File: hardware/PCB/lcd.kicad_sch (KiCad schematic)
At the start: 68 parts, among them U1 TSC2013QRSARQ1, U2 TPS923650

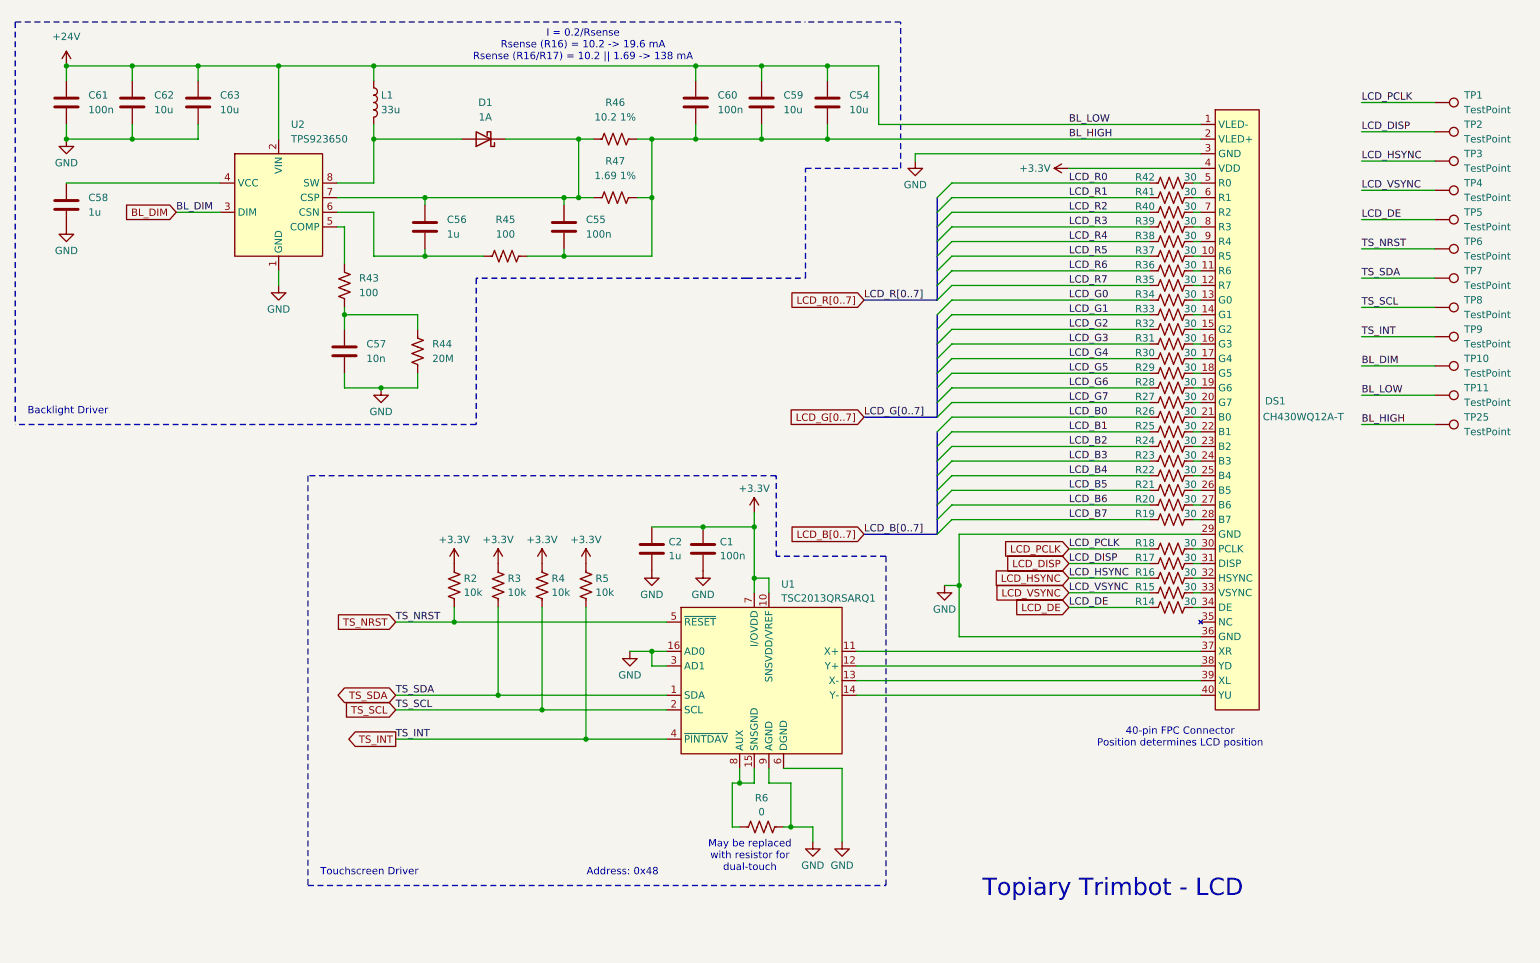
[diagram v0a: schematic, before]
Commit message: LCD schematic: small changes, add PSpice sim
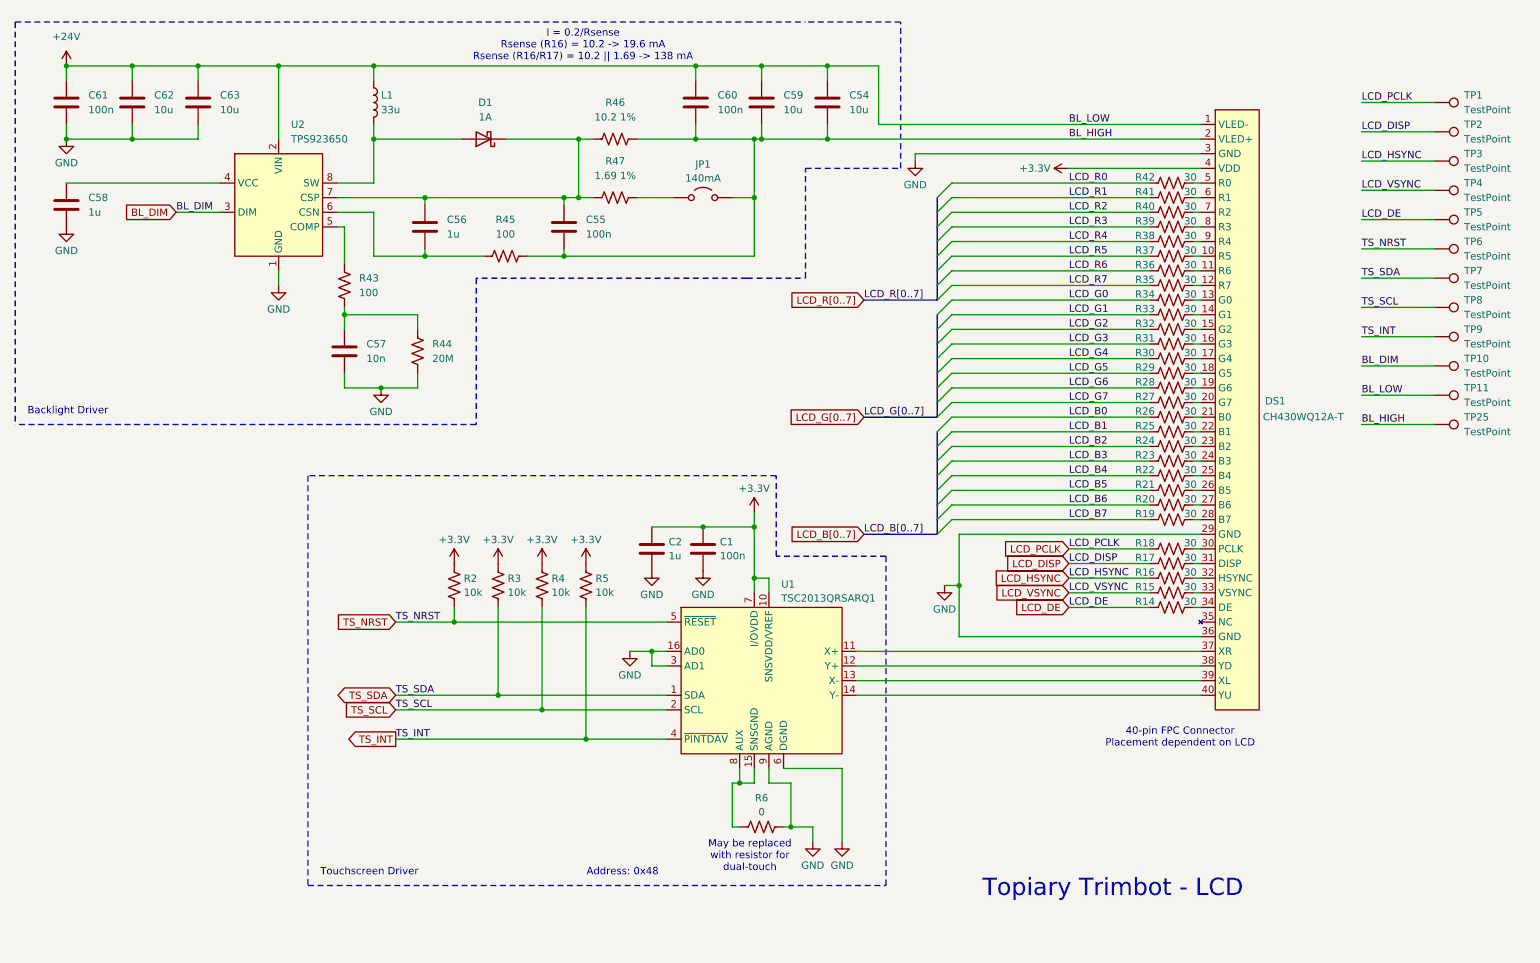
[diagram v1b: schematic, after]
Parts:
- added JP1: 140mA, symbol Jumper:Jumper_2_Open
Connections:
- net BL_HIGH: now also JP1.2 (B); no longer R47.2
- new net: JP1.1 (A), R47.2
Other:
- note added: "40-pin FPC Connector Placement dependent on LCD"
- note removed: "40-pin FPC Connector Position determines LCD position"
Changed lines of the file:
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@@
 		)
 	)
-	(text "40-pin FPC Connector\nPosition determines LCD position"
+	(text "40-pin FPC Connector\nPlacement dependent on LCD"
 		(exclude_from_sim no)
 		(at 222.504 148.336 0)
@@
 	)
 	(junction
+		(at 148.59 54.61)
+		(diameter 0)
+		(color 0 0 0 0)
+	)
+	(junction
 		(at 161.29 31.75)
 		(diameter 0)
@@
 	)
 	(junction
+		(at 148.59 44.45)
+		(diameter 0)
+		(color 0 0 0 0)
+	)
+	(junction
 		(at 118.11 44.45)
 		(diameter 0)
@@
 	)
 	(junction
-		(at 130.81 54.61)
-		(diameter 0)
-		(color 0 0 0 0)
-	)
-	(junction
 		(at 119.38 148.59)
 		(diameter 0)
@@
 	)
 	(junction
-		(at 130.81 44.45)
-		(diameter 0)
-		(color 0 0 0 0)
-	)
-	(junction
 		(at 40.64 31.75)
 		(diameter 0)
@@
 	(wire
 		(pts
-			(xy 128.27 44.45) (xy 130.81 44.45)
+			(xy 128.27 44.45) (xy 138.43 44.45)
 		)
 		(stroke
@@
 	(wire
 		(pts
+			(xy 138.43 44.45) (xy 148.59 44.45)
+		)
+		(stroke
+			(width 0)
+			(type default)
+		)
+	)
+	(wire
+		(pts
 			(xy 166.37 140.97) (xy 226.06 140.97)
 		)
@@
 	(wire
 		(pts
-			(xy 138.43 44.45) (xy 149.86 44.45)
-		)
-		(stroke
-			(width 0)
-			(type default)
-		)
-	)
-	(wire
-		(pts
 			(xy 184.15 121.92) (xy 184.15 130.81)
 		)
@@
 	(wire
 		(pts
-			(xy 115.57 64.77) (xy 130.81 64.77)
+			(xy 115.57 64.77) (xy 148.59 64.77)
 		)
 		(stroke
@@
 	(wire
 		(pts
-			(xy 130.81 44.45) (xy 138.43 44.45)
-		)
-		(stroke
-			(width 0)
-			(type default)
-		)
-	)
-	(wire
-		(pts
 			(xy 76.2 59.69) (xy 77.47 59.69)
 		)
@@
 		)
 	)
+	(wire
+		(pts
+			(xy 144.78 54.61) (xy 148.59 54.61)
+		)
+		(stroke
+			(width 0)
+			(type default)
+		)
+	)
 	(polyline
 		(pts
@@
 	(wire
 		(pts
-			(xy 130.81 54.61) (xy 130.81 44.45)
+			(xy 148.59 44.45) (xy 148.59 54.61)
 		)
 		(stroke
@@
 		)
 	)
+	(wire
+		(pts
+			(xy 148.59 44.45) (xy 149.86 44.45)
+		)
+		(stroke
+			(width 0)
+			(type default)
+		)
+	)
 	(bus
 		(pts
@@
 	(wire
 		(pts
+			(xy 148.59 54.61) (xy 148.59 64.77)
+		)
+		(stroke
+			(width 0)
+			(type default)
+		)
+	)
+	(wire
+		(pts
 			(xy 224.79 105.41) (xy 226.06 105.41)
 		)
@@
 	(wire
 		(pts
-			(xy 130.81 64.77) (xy 130.81 54.61)
-		)
-		(stroke
-			(width 0)
-			(type default)
-		)
-	)
-	(wire
-		(pts
 			(xy 77.47 73.66) (xy 77.47 74.93)
 		)
@@
 		)
 	)
-	(wire
-		(pts
-			(xy 128.27 54.61) (xy 130.81 54.61)
-		)
-		(stroke
-			(width 0)
-			(type default)
-		)
-	)
 	(polyline
 		(pts
@@
 	(wire
 		(pts
+			(xy 128.27 54.61) (xy 134.62 54.61)
+		)
+		(stroke
+			(width 0)
+			(type default)
+		)
+	)
+	(wire
+		(pts
 			(xy 148.59 111.76) (xy 148.59 120.65)
 		)
@@
 					(unit 1)
 				)
+			)
+		)
+	)
+	(symbol
+		(lib_id "Jumper:Jumper_2_Open")
+		(at 139.7 54.61 0)
+		(unit 1)
+		(exclude_from_sim no)
+		(in_bom yes)
+		(on_board yes)
+		(dnp no)
+		(fields_autoplaced yes)
+		(property "Reference" "JP1"
+			(at 139.7 48.8145 0)
+			(effects
+				(font
+					(size 1.27 1.27)
+				)
+			)
+		)
+		(property "Value" "140mA"
+			(at 139.7 51.2388 0)
+			(effects
+				(font
+					(size 1.27 1.27)
+				)
+			)
+		)
+		(property "Footprint" ""
+			(at 139.7 54.61 0)
+			(effects
+				(font
+					(size 1.27 1.27)
+				)
+				(hide yes)
+			)
+		)
+		(property "Datasheet" "~"
+			(at 139.7 54.61 0)
+			(effects
+				(font
+					(size 1.27 1.27)
+				)
+				(hide yes)
+			)
+		)
+		(property "Description" "Jumper, 2-pole, open"
+			(at 139.7 54.61 0)
+			(effects
+				(font
+					(size 1.27 1.27)
+				)
+				(hide yes)
+			)
+		)
+		(pin "2"
+		)
+		(pin "1"
+		)
+		(instances
+			(project ""
+				(path "/2826ff7c-9767-4078-8ea2-1cd3a432abf3/e982bc10-c57a-42ac-b92d-a536dd69a0fd"
+					(reference "JP1")
+					(unit 1)
+				)

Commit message: LCD schematic: more small additions and set footprints for all components
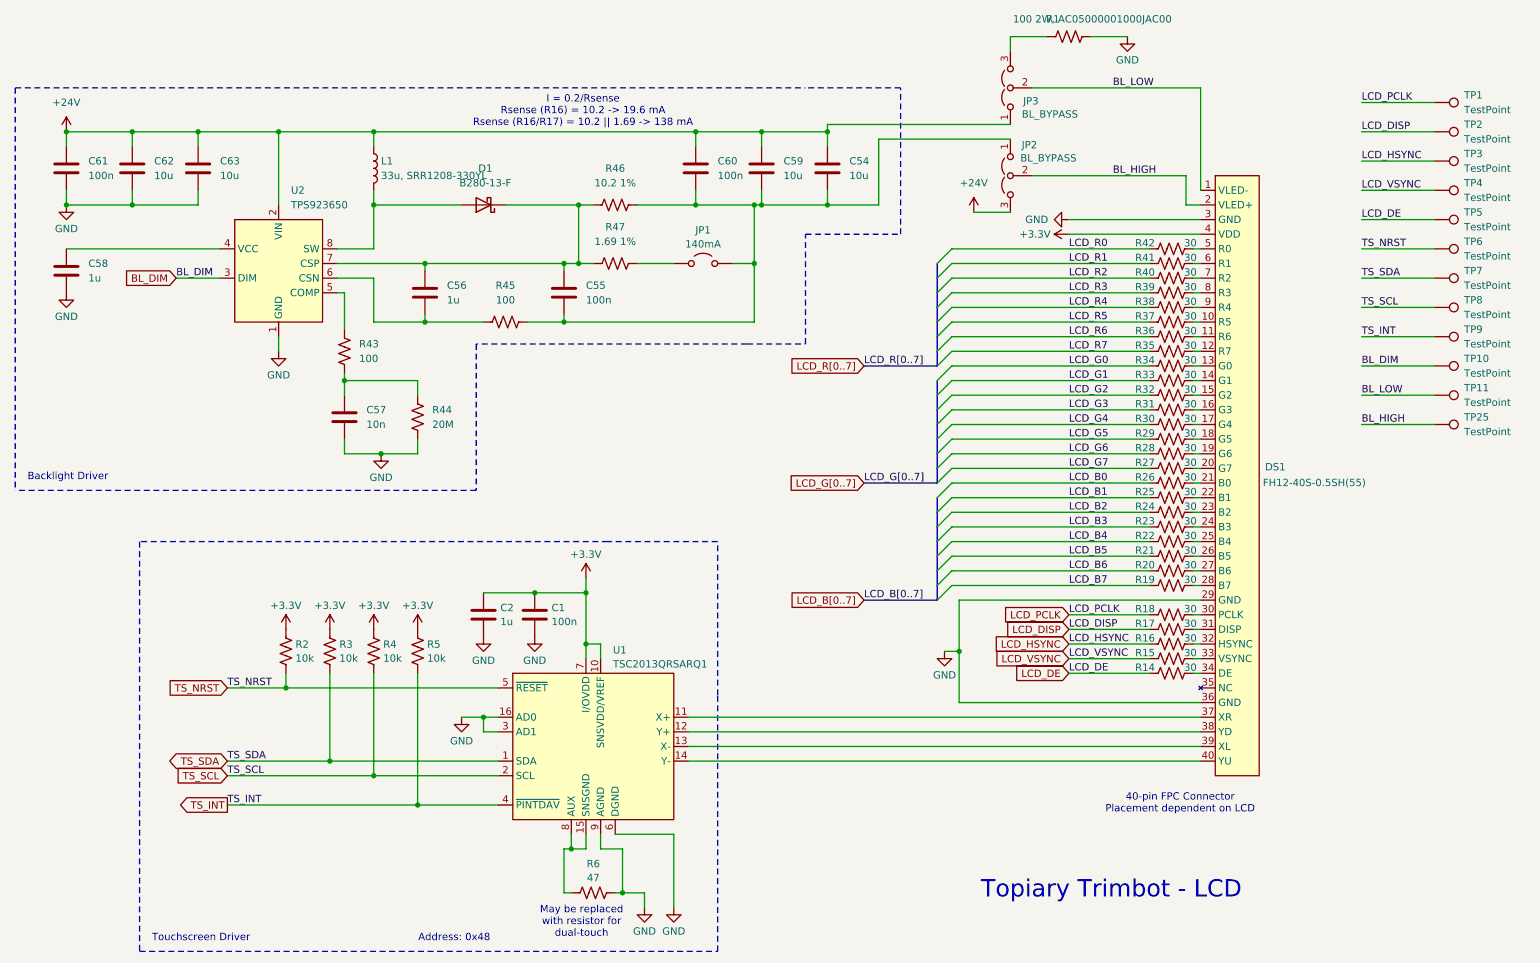
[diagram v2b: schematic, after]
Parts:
- added JP2, JP3: BL_BYPASS, Connector_PinHeader_2.54mm:PinHeader_1x03_P2.54mm_Vertical, symbol Jumper:Jumper_3_Open
- added R1: 100 2W, AC05000001000JAC00, Resistor_THT:R_Axial_DIN0918_L18.0mm_D9.0mm_P25.40mm_Horizontal, symbol Device:R_US
- C1, C2, C55, C56, C57, C58, C60, C61: footprint (none) -> Capacitor_SMD:C_0603_1608Metric
- C54, C59, C62, C63: footprint (none) -> Capacitor_SMD:C_0805_2012Metric
- D1: value 1A -> B280-13-F; footprint (none) -> Diode_SMD:D_SMB
- DS1: value CH430WQ12A-T -> FH12-40S-0.5SH(55); footprint (none) -> Connector_FFC-FPC:Hirose_FH12-40S-0.5SH_1x40-1MP_P0.50mm_Horizontal
- JP1: footprint (none) -> Connector_PinHeader_2.54mm:PinHeader_1x02_P2.54mm_Vertical
- L1: value 33u -> 33u, SRR1208-330YL; footprint (none) -> Inductor_SMD:L_Bourns_SRR1208_12.7x12.7mm
- R14, R15, R16, R17, R18, R19, R20, R21, R22, R23, R24, R25, R26, R27, R28, R29, R30, R31, R32, R33, R34, R35, R36, R37, R38, R39, R40, R41, R42, R43, R44, R45: footprint (none) -> Resistor_SMD:R_0603_1608Metric
- R2, R3, R4, R46, R47, R5: footprint (none) -> Resistor_SMD:R_0805_2012Metric
- R6: value 0 -> 47
- TP1, TP10, TP11, TP2, TP25, TP3, TP4, TP5, TP6, TP7, TP8, TP9: footprint (none) -> TestPoint:TestPoint_Pad_D1.5mm
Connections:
- net +24V: now also JP2.3 (B), JP3.1 (A); no longer DS1.1 (VLED-), TP11.1
- net BL_HIGH: now also JP2.2 (C); no longer C54.2, C55.2, C59.2, C60.2, JP1.2 (B), R45.2, R46.2
- net GND: now also R1.2
- new net: C54.2, C55.2, C59.2, C60.2, JP1.2 (B), JP2.1 (A), R45.2, R46.2
- new net: JP3.3 (B), R1.1
- new net BL_LOW: DS1.1 (VLED-), JP3.2 (C), TP11.1
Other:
- moved on the sheet: C1, C2, C54, C55, C56, C57, C58, C59, C60, C61, C62, C63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

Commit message: Schematic: add manufacturer PN field and start picking parts and footprints in LCD and Motor
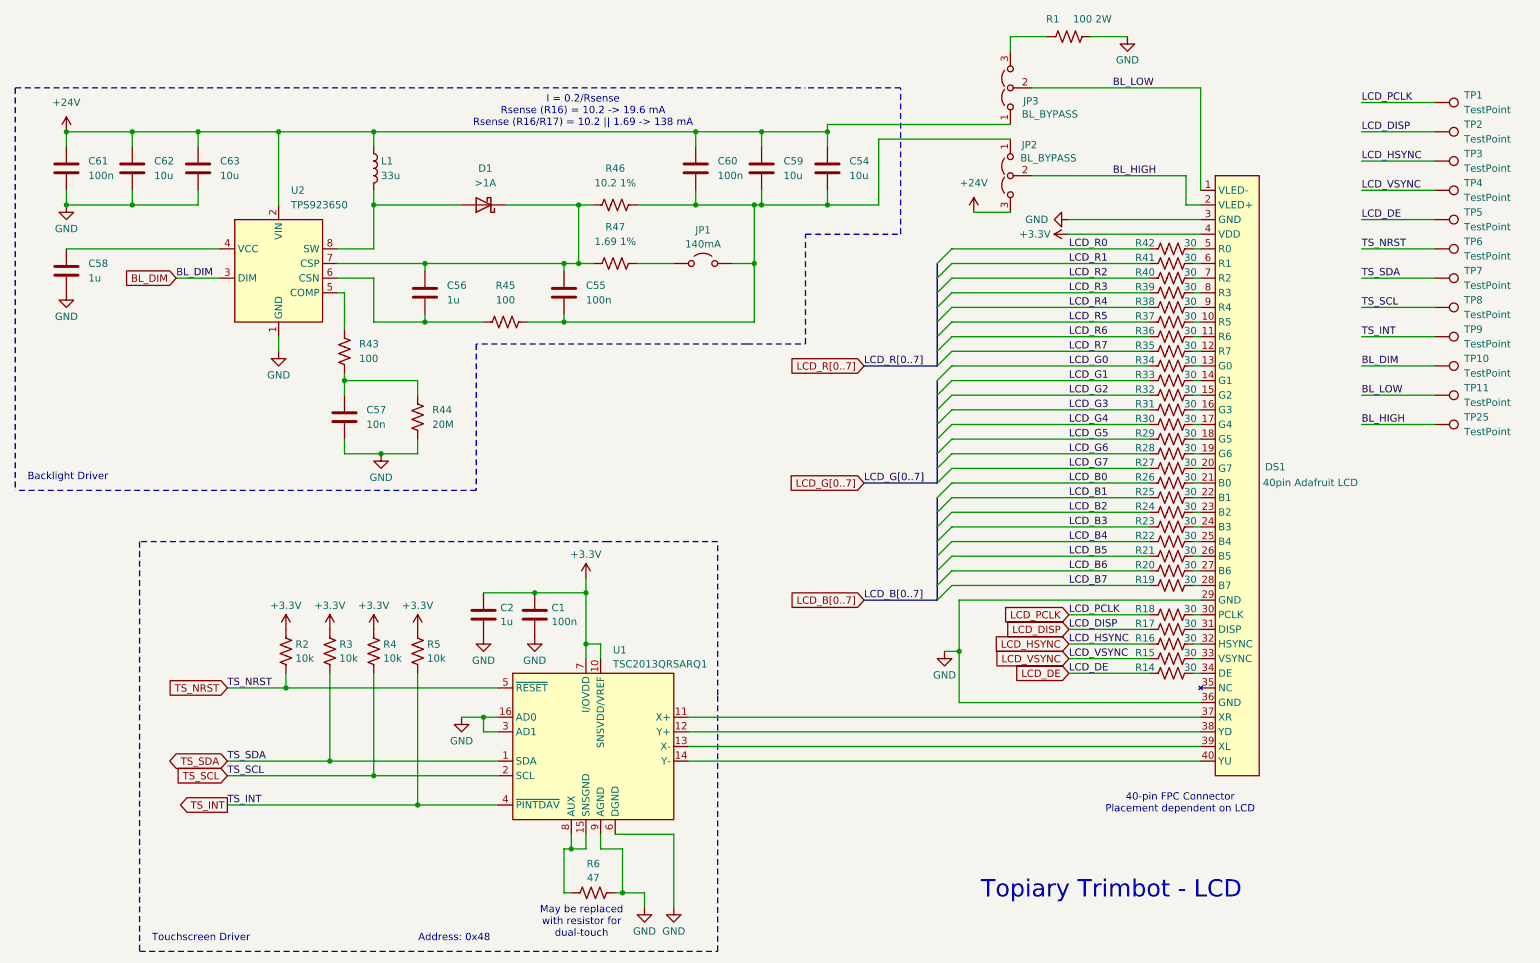
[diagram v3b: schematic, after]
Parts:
- D1: value B280-13-F -> >1A; Manufacturer_Part_Number (none) -> B280-13-F
- DS1: value FH12-40S-0.5SH(55) -> 40pin Adafruit LCD; Manufacturer_Part_Number (none) -> FH12-40S-0.5SH(55)
- L1: value 33u, SRR1208-330YL -> 33u; Manufacturer_Part_Number (none) -> SRR1208-330YL
- R1: value 100 2W, AC05000001000JAC00 -> 100 2W; Manufacturer_Part_Number (none) -> AC05000001000JAC00
- U1: Manufacturer_Part_Number (none) -> TSC2013QRSARQ1
- U2: Manufacturer_Part_Number (none) -> TPS923650

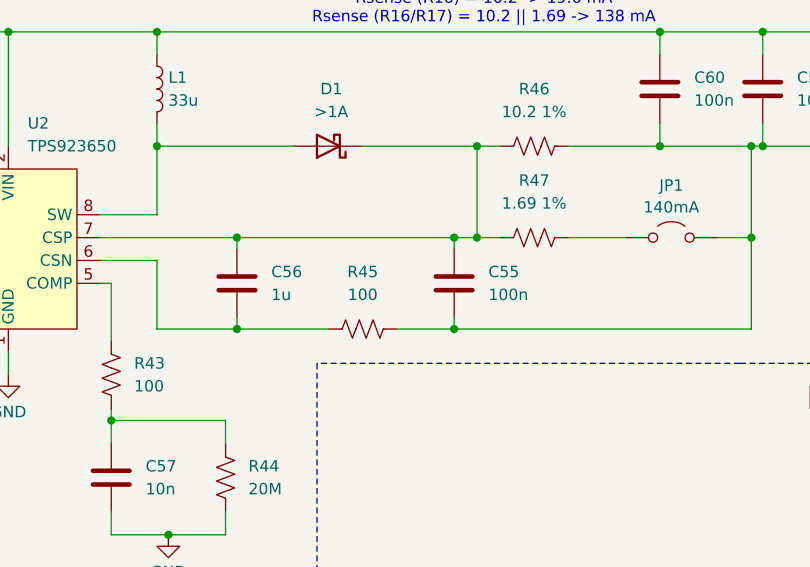
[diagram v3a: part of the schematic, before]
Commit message: Schematic: change capacitor in backlight feedback according to sims, add oscillator symbol/footprint
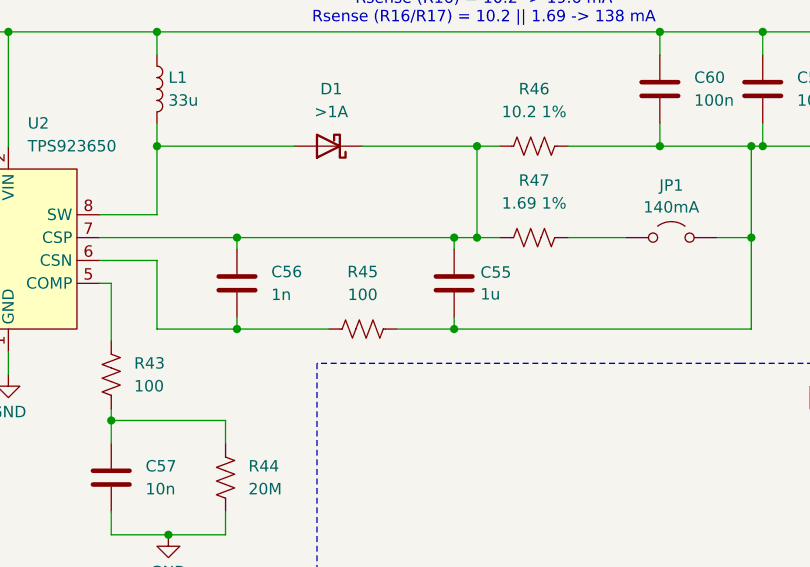
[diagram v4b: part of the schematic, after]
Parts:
- C55: value 100n -> 1u
- C56: value 1u -> 1n
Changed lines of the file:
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@@
 		(fields_autoplaced yes)
 		(property "Reference" "C55"
-			(at 119.38 69.8499 0)
-			(effects
-				(font
-					(size 1.27 1.27)
-				)
-				(justify left)
-			)
-		)
-		(property "Value" "100n"
-			(at 119.38 72.3899 0)
+			(at 118.491 69.9078 0)
+			(effects
+				(font
+					(size 1.27 1.27)
+				)
+				(justify left)
+			)
+		)
+		(property "Value" "1u"
+			(at 118.491 72.3321 0)
 			(effects
 				(font
@@
 			)
 		)
-		(property "Value" "1u"
+		(property "Value" "1n"
 			(at 95.25 72.3899 0)
 			(effects
